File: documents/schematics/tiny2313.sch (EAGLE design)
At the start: 14 parts, among them Q1 20 MHz, Q2 BS170, Q3 BS170

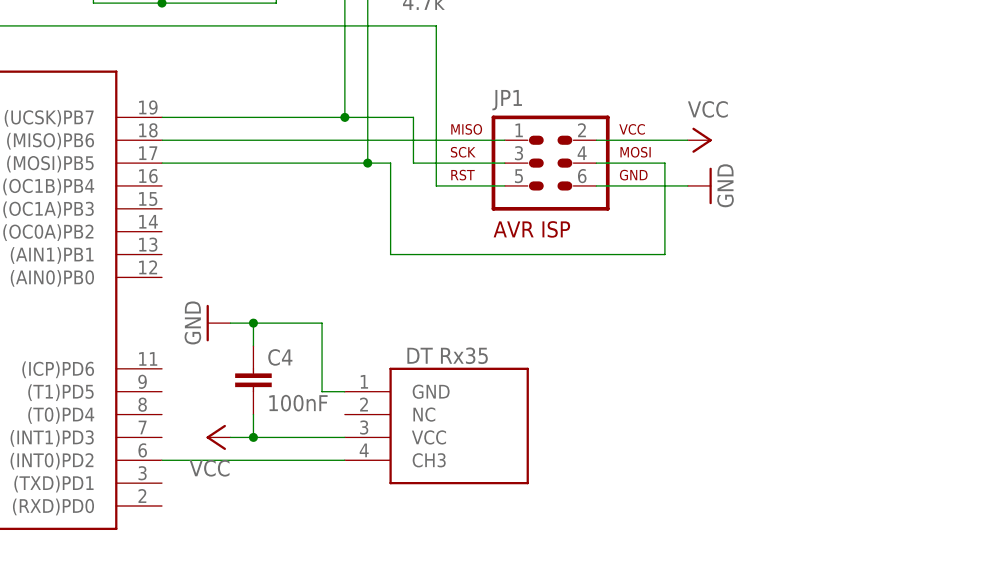
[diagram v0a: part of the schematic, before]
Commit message: RX12 receiver can now be en-/disabled via I2C
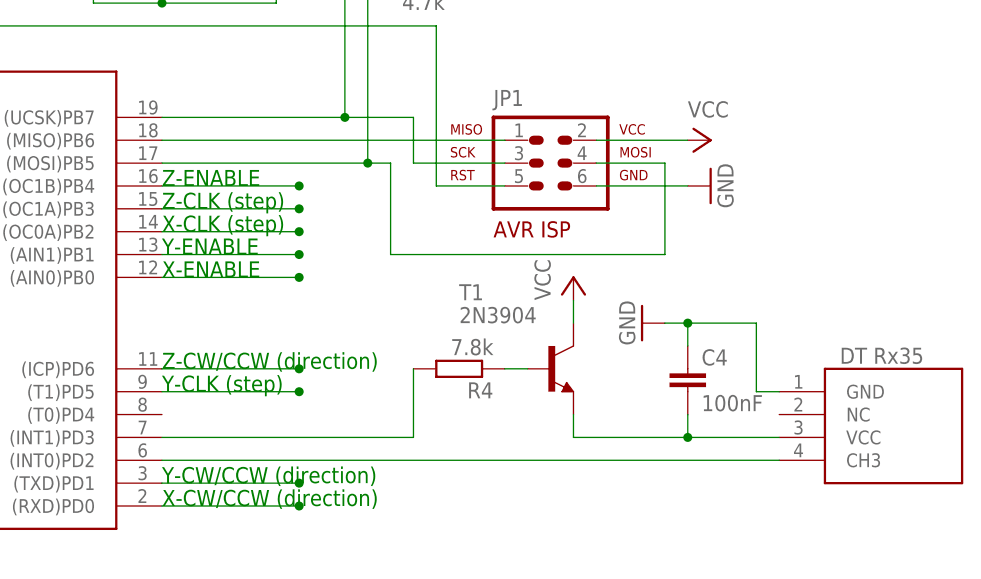
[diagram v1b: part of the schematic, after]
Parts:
- added R4: 7.8k, resistor:R-EU_0207/12
- added T1: 2N3904, transistor-npn:2N3904
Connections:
- new net N$10: U$1.(AIN1)PB1
- new net N$11: U$1.(AIN0)PB0
- new net N$12: U$1.(ICP)PD6
- new net N$13: U$1.(TXD)PD1
- new net N$14: U$1.(RXD)PD0
- new net N$15: R4.1, T1.B
- new net N$17: C4.2, T1.E, U$2.VCC
- new net N$18: R4.2, U$1.(INT1)PD3
- new net N$6: U$1.(T1)PD5
- new net N$7: U$1.(OC0A)PB2
- new net N$8: U$1.(OC1A)PB3
- new net N$9: U$1.(OC1B)PB4
- net VCC: now also T1.C; no longer C4.2, U$2.VCC
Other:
- note added: "X-CLK (step)"
- note added: "X-CW/CCW (direction)"
- note added: "X-ENABLE"
- note added: "Y-CLK (step)"
- note added: "Y-CW/CCW (direction)"
- note added: "Y-ENABLE"
- note added: "Z-CLK (step)"
- note added: "Z-CW/CCW (direction)"
- note added: "Z-ENABLE"
- moved on the sheet: C4
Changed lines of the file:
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@@
 <part name="GND6" library="supply1" deviceset="GND" device=""/>
 <part name="U$2" library="DTRX35" deviceset="DTRX35" device=""/>
-<part name="P+9" library="supply1" deviceset="VCC" device=""/>
 <part name="GND11" library="supply1" deviceset="GND" device=""/>
 <part name="C4" library="capacitor-wima" deviceset="C" device="2.5/2" value="100nF"/>
@@
 <part name="Q3" library="transistor-small-signal" deviceset="BS170" device=""/>
 <part name="GPIO" library="con-ml" deviceset="ML26" device=""/>
+<part name="T1" library="transistor-npn" deviceset="2N3904" device=""/>
+<part name="P+1" library="supply1" deviceset="VCC" device=""/>
+<part name="R4" library="resistor" deviceset="R-EU_" device="0207/12" value="7.8k"/>
 </parts>
 <sheets>
 <sheet>
 <plain>
+<text x="76.2" y="73.66" size="1.778" layer="91">X-CLK (step) </text>
+<text x="76.2" y="55.88" size="1.778" layer="91">Y-CLK (step)</text>
+<text x="76.2" y="76.2" size="1.778" layer="91">Z-CLK (step)</text>
+<text x="76.2" y="68.58" size="1.778" layer="91">X-ENABLE</text>
+<text x="76.2" y="71.12" size="1.778" layer="91">Y-ENABLE</text>
+<text x="76.2" y="78.74" size="1.778" layer="91">Z-ENABLE</text>
+<text x="76.2" y="43.18" size="1.778" layer="91">X-CW/CCW (direction)</text>
+<text x="76.2" y="45.72" size="1.778" layer="91">Y-CW/CCW (direction)</text>
+<text x="76.2" y="58.42" size="1.778" layer="91">Z-CW/CCW (direction)</text>
 </plain>
 <instances>
@@
 <instance part="P+3" gate="VCC" x="20.32" y="50.8" rot="R90"/>
 <instance part="GND6" gate="1" x="20.32" y="43.18" rot="R270"/>
-<instance part="U$2" gate="G$1" x="101.6" y="50.8"/>
-<instance part="P+9" gate="VCC" x="81.28" y="50.8" rot="R90"/>
-<instance part="GND11" gate="1" x="81.28" y="63.5" rot="R270"/>
-<instance part="C4" gate="G$1" x="86.36" y="58.42"/>
+<instance part="U$2" gate="G$1" x="149.86" y="50.8"/>
+<instance part="GND11" gate="1" x="129.54" y="63.5" rot="R270"/>
+<instance part="C4" gate="G$1" x="134.62" y="58.42"/>
 <instance part="JP1" gate="G$1" x="119.38" y="81.28"/>
 <instance part="GND7" gate="1" x="137.16" y="78.74" rot="MR270"/>
@@
 <instance part="Q3" gate="1" x="76.2" y="109.22" rot="R90"/>
 <instance part="GPIO" gate="1" x="58.42" y="121.92"/>
+<instance part="T1" gate="G1" x="119.38" y="58.42"/>
+<instance part="P+1" gate="VCC" x="121.92" y="68.58"/>
+<instance part="R4" gate="G$1" x="109.22" y="58.42" rot="R180"/>
 </instances>
 <busses>
@@
 <nets>
 <net name="VCC" class="0">
-<segment>
-<pinref part="P+9" gate="VCC" pin="VCC"/>
-<pinref part="U$2" gate="G$1" pin="VCC"/>
-<wire x1="83.82" y1="50.8" x2="86.36" y2="50.8" width="0.1524" layer="91"/>
-<pinref part="C4" gate="G$1" pin="2"/>
-<wire x1="86.36" y1="50.8" x2="96.52" y2="50.8" width="0.1524" layer="91"/>
-<wire x1="86.36" y1="53.34" x2="86.36" y2="50.8" width="0.1524" layer="91"/>
-<junction x="86.36" y="50.8"/>
-</segment>
 <segment>
 <pinref part="JP1" gate="G$1" pin="2"/>
@@
 <pinref part="P+10" gate="VCC" pin="VCC"/>
 </segment>
+<segment>
+<pinref part="P+1" gate="VCC" pin="VCC"/>
+<pinref part="T1" gate="G1" pin="C"/>
+<wire x1="121.92" y1="66.04" x2="121.92" y2="63.5" width="0.1524" layer="91"/>
+</segment>
 </net>
 <net name="GND" class="0">
@@
 <pinref part="GND11" gate="1" pin="GND"/>
 <pinref part="C4" gate="G$1" pin="1"/>
-<wire x1="83.82" y1="63.5" x2="86.36" y2="63.5" width="0.1524" layer="91"/>
-<wire x1="86.36" y1="60.96" x2="86.36" y2="63.5" width="0.1524" layer="91"/>
-<wire x1="86.36" y1="63.5" x2="93.98" y2="63.5" width="0.1524" layer="91"/>
-<wire x1="93.98" y1="63.5" x2="93.98" y2="55.88" width="0.1524" layer="91"/>
+<wire x1="132.08" y1="63.5" x2="134.62" y2="63.5" width="0.1524" layer="91"/>
+<wire x1="134.62" y1="60.96" x2="134.62" y2="63.5" width="0.1524" layer="91"/>
+<wire x1="134.62" y1="63.5" x2="142.24" y2="63.5" width="0.1524" layer="91"/>
+<wire x1="142.24" y1="63.5" x2="142.24" y2="55.88" width="0.1524" layer="91"/>
 <pinref part="U$2" gate="G$1" pin="GND"/>
-<wire x1="93.98" y1="55.88" x2="96.52" y2="55.88" width="0.1524" layer="91"/>
-<junction x="86.36" y="63.5"/>
+<wire x1="142.24" y1="55.88" x2="144.78" y2="55.88" width="0.1524" layer="91"/>
+<junction x="134.62" y="63.5"/>
 </segment>
 <segment>
@@
 <segment>
 <pinref part="U$1" gate="G$1" pin="(INT0)PD2"/>
-<wire x1="76.2" y1="48.26" x2="96.52" y2="48.26" width="0.1524" layer="91"/>
+<wire x1="76.2" y1="48.26" x2="144.78" y2="48.26" width="0.1524" layer="91"/>
 <pinref part="U$2" gate="G$1" pin="CH3"/>
 </segment>
@@
 </segment>
 </net>
+<net name="N$6" class="0">
+<segment>
+<pinref part="U$1" gate="G$1" pin="(T1)PD5"/>
+<wire x1="76.2" y1="55.88" x2="91.44" y2="55.88" width="0.1524" layer="91"/>
+<junction x="91.44" y="55.88"/>
+</segment>
+</net>
+<net name="N$7" class="0">
+<segment>
+<pinref part="U$1" gate="G$1" pin="(OC0A)PB2"/>
+<wire x1="76.2" y1="73.66" x2="91.44" y2="73.66" width="0.1524" layer="91"/>
+<junction x="91.44" y="73.66"/>
+</segment>
+</net>
+<net name="N$8" class="0">
+<segment>
+<pinref part="U$1" gate="G$1" pin="(OC1A)PB3"/>
+<wire x1="76.2" y1="76.2" x2="91.44" y2="76.2" width="0.1524" layer="91"/>
+<junction x="91.44" y="76.2"/>
+</segment>
+</net>
+<net name="N$9" class="0">
+<segment>
+<pinref part="U$1" gate="G$1" pin="(OC1B)PB4"/>
+<wire x1="76.2" y1="78.74" x2="91.44" y2="78.74" width="0.1524" layer="91"/>
+<junction x="91.44" y="78.74"/>
+</segment>
+</net>
+<net name="N$10" class="0">
+<segment>
+<pinref part="U$1" gate="G$1" pin="(AIN1)PB1"/>
+<wire x1="76.2" y1="71.12" x2="91.44" y2="71.12" width="0.1524" layer="91"/>
+<junction x="91.44" y="71.12"/>
+</segment>
+</net>
+<net name="N$11" class="0">
+<segment>
+<pinref part="U$1" gate="G$1" pin="(AIN0)PB0"/>
+<wire x1="76.2" y1="68.58" x2="91.44" y2="68.58" width="0.1524" layer="91"/>
+<junction x="91.44" y="68.58"/>
+</segment>
+</net>
+<net name="N$12" class="0">
+<segment>
+<pinref part="U$1" gate="G$1" pin="(ICP)PD6"/>
+<wire x1="76.2" y1="58.42" x2="91.44" y2="58.42" width="0.1524" layer="91"/>
+<junction x="91.44" y="58.42"/>
+</segment>
+</net>
+<net name="N$13" class="0">
+<segment>
+<pinref part="U$1" gate="G$1" pin="(TXD)PD1"/>
+<wire x1="76.2" y1="45.72" x2="91.44" y2="45.72" width="0.1524" layer="91"/>
+<junction x="91.44" y="45.72"/>
+</segment>
+</net>
+<net name="N$14" class="0">
+<segment>
+<pinref part="U$1" gate="G$1" pin="(RXD)PD0"/>
+<wire x1="76.2" y1="43.18" x2="91.44" y2="43.18" width="0.1524" layer="91"/>
+<junction x="91.44" y="43.18"/>
+</segment>
+</net>
+<net name="N$17" class="0">
+<segment>
+<pinref part="U$2" gate="G$1" pin="VCC"/>
+<pinref part="C4" gate="G$1" pin="2"/>
+<wire x1="134.62" y1="50.8" x2="144.78" y2="50.8" width="0.1524" layer="91"/>
+<wire x1="134.62" y1="53.34" x2="134.62" y2="50.8" width="0.1524" layer="91"/>
+<pinref part="T1" gate="G1" pin="E"/>
+<wire x1="121.92" y1="53.34" x2="121.92" y2="50.8" width="0.1524" layer="91"/>
+<wire x1="121.92" y1="50.8" x2="134.62" y2="50.8" width="0.1524" layer="91"/>
+<junction x="134.62" y="50.8"/>
+</segment>
+</net>
+<net name="N$15" class="0">
+<segment>
+<pinref part="R4" gate="G$1" pin="1"/>
+<pinref part="T1" gate="G1" pin="B"/>
+<wire x1="114.3" y1="58.42" x2="116.84" y2="58.42" width="0.1524" layer="91"/>
+</segment>
+</net>
+<net name="N$18" class="0">
+<segment>
+<pinref part="R4" gate="G$1" pin="2"/>
+<wire x1="104.14" y1="58.42" x2="104.14" y2="50.8" width="0.1524" layer="91"/>
+<pinref part="U$1" gate="G$1" pin="(INT1)PD3"/>
+<wire x1="104.14" y1="50.8" x2="76.2" y2="50.8" width="0.1524" layer="91"/>
+</segment>
+</net>
